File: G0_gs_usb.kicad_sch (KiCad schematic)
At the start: 59 parts, among them J1 USB_C_Receptacle_USB2.0, J12 CAN1, J13 CAN2, J4 Conn_01x03_Pin, SW1 SW_Push_Dual, U1 STM32G0B1CBTx, U2 TJA1042T-3, U3 TJA1042T-3, U4 XC6206PxxxMR

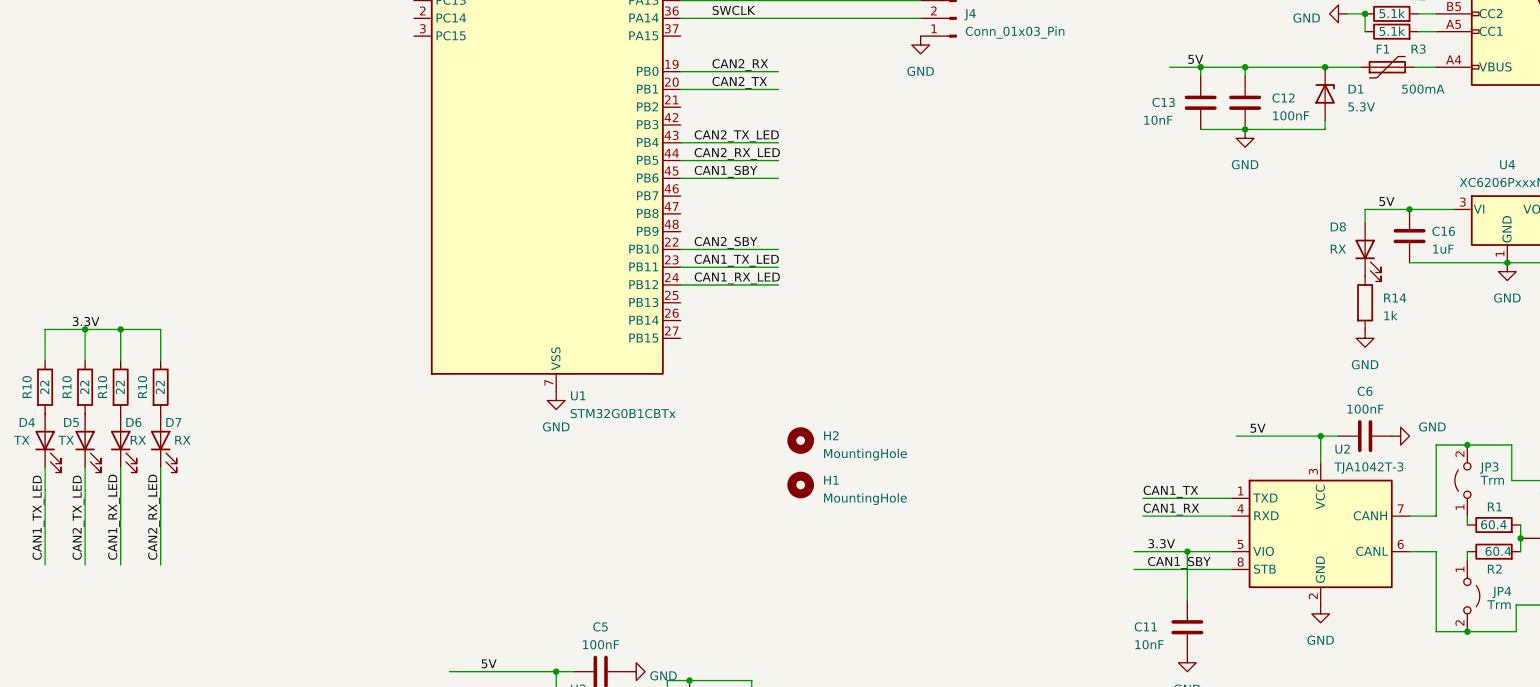
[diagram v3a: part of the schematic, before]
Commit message: Update net labels to match the purpose of the pins.
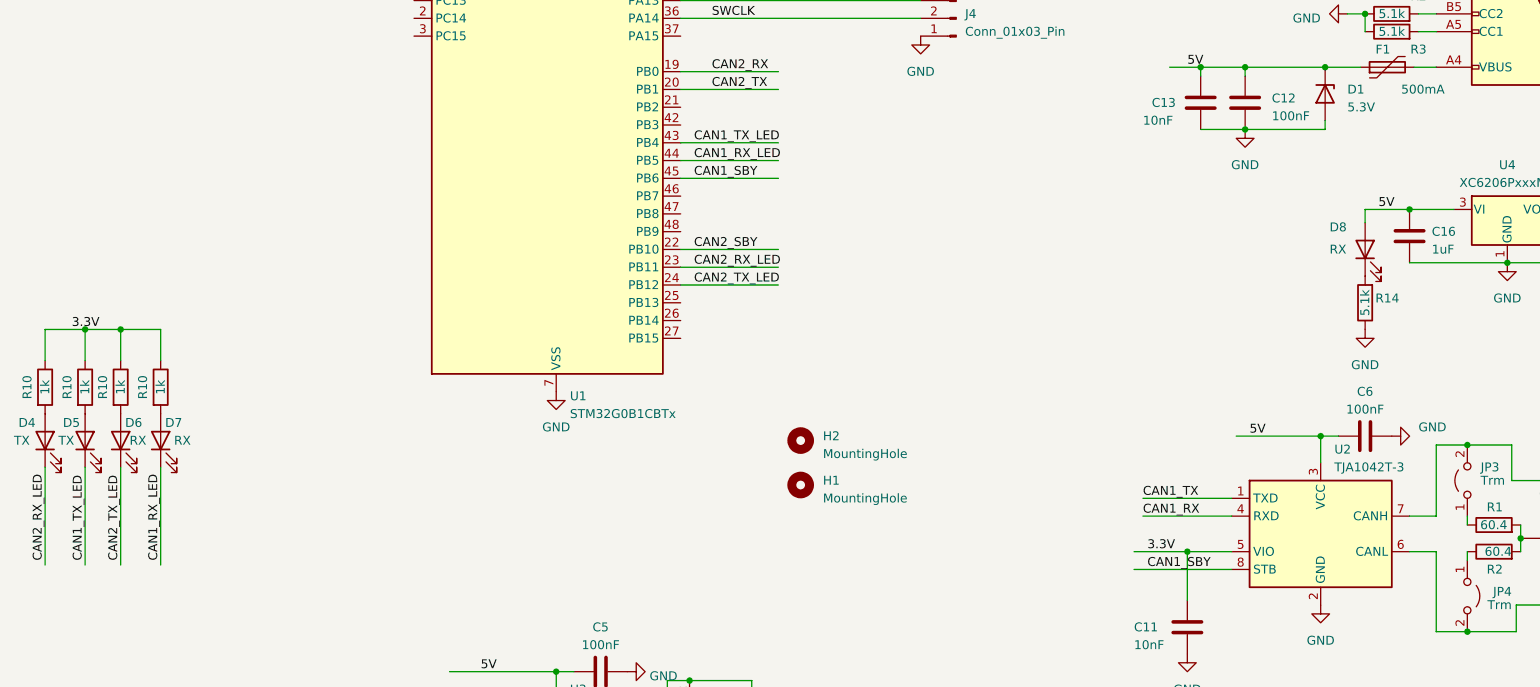
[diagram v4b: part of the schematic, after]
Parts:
- R10: value 22 -> 1k; LCSC Part # C25092 -> C11702; Part # 0402WGF220JTCE -> 0402WGF1001TCE
- R14: value 1k -> 5.1k; LCSC Part # C11702 -> C11616; Part # 0402WGF1001TCE -> 0402WGF5103TCE
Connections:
- net CAN1_RX_LED: now also D7.1 (K), U1.44 (PB5); no longer D6.1 (K), U1.24 (PB12)
- net CAN1_TX_LED: now also D5.1 (K), U1.43 (PB4); no longer D4.1 (K), U1.23 (PB11)
- net CAN2_RX_LED: now also D4.1 (K), U1.23 (PB11); no longer D7.1 (K), U1.44 (PB5)
- net CAN2_TX_LED: now also D6.1 (K), U1.24 (PB12); no longer D5.1 (K), U1.43 (PB4)
- net GND: now also R14.1; no longer R14.2
- net at D8.1 (K): now also R14.2; no longer R14.1
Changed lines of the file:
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@@
     (effects (font (size 1.27 1.27)) (justify left bottom))
   )
-  (label "CAN1_RX_LED" (at 39.37 144.145 90) (fields_autoplaced)
+  (label "CAN2_TX_LED" (at 39.37 144.145 90) (fields_autoplaced)
     (effects (font (size 1.27 1.27)) (justify left bottom))
   )
@@
     (effects (font (size 1.27 1.27)) (justify left bottom))
   )
-  (label "CAN2_RX_LED" (at 121.285 86.995 0) (fields_autoplaced)
+  (label "CAN1_RX_LED" (at 121.285 86.995 0) (fields_autoplaced)
     (effects (font (size 1.27 1.27)) (justify left bottom))
   )
@@
     (effects (font (size 1.27 1.27)) (justify left bottom))
   )
-  (label "CAN2_TX_LED" (at 121.285 84.455 0) (fields_autoplaced)
+  (label "CAN1_TX_LED" (at 121.285 84.455 0) (fields_autoplaced)
     (effects (font (size 1.27 1.27)) (justify left bottom))
   )
@@
     (effects (font (size 1.27 1.27)) (justify left bottom))
   )
-  (label "CAN1_TX_LED" (at 121.285 102.235 0) (fields_autoplaced)
+  (label "CAN2_RX_LED" (at 121.285 102.235 0) (fields_autoplaced)
     (effects (font (size 1.27 1.27)) (justify left bottom))
   )
@@
     (effects (font (size 1.27 1.27)) (justify left bottom))
   )
-  (label "CAN1_TX_LED" (at 28.575 144.145 90) (fields_autoplaced)
+  (label "CAN2_RX_LED" (at 28.575 144.145 90) (fields_autoplaced)
     (effects (font (size 1.27 1.27)) (justify left bottom))
   )
@@
     (effects (font (size 1.27 1.27)) (justify left bottom))
   )
-  (label "CAN2_TX_LED" (at 34.29 144.145 90) (fields_autoplaced)
-    (effects (font (size 1.27 1.27)) (justify left bottom))
-  )
-  (label "CAN1_RX_LED" (at 121.285 104.775 0) (fields_autoplaced)
+  (label "CAN1_TX_LED" (at 34.29 144.145 90) (fields_autoplaced)
+    (effects (font (size 1.27 1.27)) (justify left bottom))
+  )
+  (label "CAN2_TX_LED" (at 121.285 104.775 0) (fields_autoplaced)
     (effects (font (size 1.27 1.27)) (justify left bottom))
   )
@@
     (effects (font (size 1.27 1.27)) (justify left bottom))
   )
-  (label "CAN2_RX_LED" (at 45.085 144.145 90) (fields_autoplaced)
+  (label "CAN1_RX_LED" (at 45.085 144.145 90) (fields_autoplaced)
     (effects (font (size 1.27 1.27)) (justify left bottom))
   )
@@
       (effects (font (size 1.27 1.27)))
     )
-    (property "Value" "22" (at 28.575 119.38 90)
+    (property "Value" "1k" (at 28.575 119.38 90)
       (effects (font (size 1.27 1.27)))
     )
@@
       (effects (font (size 1.27 1.27)) hide)
     )
-    (property "Part #" "0402WGF220JTCE" (at 28.575 119.38 0)
-      (effects (font (size 1.27 1.27)) hide)
-    )
-    (property "LCSC Part #" "C25092" (at 28.575 119.38 0)
+    (property "Part #" "0402WGF1001TCE" (at 28.575 119.38 0)
+      (effects (font (size 1.27 1.27)) hide)
+    )
+    (property "LCSC Part #" "C11702" (at 28.575 119.38 0)
       (effects (font (size 1.27 1.27)) hide)
     )
@@
         (path "/c48c3db2-f9af-4991-ad00-70b882fee956"
           (reference "R10") (unit 1)
-        )
-      )
-    )
-  )
-  (symbol (lib_id "Device:R") (at 217.17 107.315 0) (unit 1)
-    (in_bom yes) (on_board yes) (dnp no) (fields_autoplaced)
-    (property "Reference" "R14" (at 219.71 106.68 0)
-      (effects (font (size 1.27 1.27)) (justify left))
-    )
-    (property "Value" "1k" (at 219.71 109.22 0)
-      (effects (font (size 1.27 1.27)) (justify left))
-    )
-    (property "Footprint" "Resistor_SMD:R_0402_1005Metric" (at 215.392 107.315 90)
-      (effects (font (size 1.27 1.27)) hide)
-    )
-    (property "Datasheet" "~" (at 217.17 107.315 0)
-      (effects (font (size 1.27 1.27)) hide)
-    )
-    (property "LCSC Part #" "C11702" (at 217.17 107.315 0)
-      (effects (font (size 1.27 1.27)) hide)
-    )
-    (property "Part #" "0402WGF1001TCE" (at 217.17 107.315 0)
-      (effects (font (size 1.27 1.27)) hide)
-    )
-    (pin "1")
-    (pin "2")
-    (instances
-      (project "G0_gs_usb"
-        (path "/c48c3db2-f9af-4991-ad00-70b882fee956"
-          (reference "R14") (unit 1)
         )
       )
@@
       (effects (font (size 1.27 1.27)))
     )
-    (property "Value" "22" (at 39.37 119.38 90)
+    (property "Value" "1k" (at 39.37 119.38 90)
       (effects (font (size 1.27 1.27)))
     )
@@
       (effects (font (size 1.27 1.27)) hide)
     )
-    (property "Part #" "0402WGF220JTCE" (at 39.37 119.38 0)
-      (effects (font (size 1.27 1.27)) hide)
-    )
-    (property "LCSC Part #" "C25092" (at 39.37 119.38 0)
+    (property "Part #" "0402WGF1001TCE" (at 39.37 119.38 0)
+      (effects (font (size 1.27 1.27)) hide)
+    )
+    (property "LCSC Part #" "C11702" (at 39.37 119.38 0)
       (effects (font (size 1.27 1.27)) hide)
     )
@@
       (effects (font (size 1.27 1.27)))
     )
-    (property "Value" "22" (at 34.29 119.38 90)
+    (property "Value" "1k" (at 34.29 119.38 90)
       (effects (font (size 1.27 1.27)))
     )
@@
       (effects (font (size 1.27 1.27)) hide)
     )
-    (property "Part #" "0402WGF220JTCE" (at 34.29 119.38 0)
-      (effects (font (size 1.27 1.27)) hide)
-    )
-    (property "LCSC Part #" "C25092" (at 34.29 119.38 0)
+    (property "Part #" "0402WGF1001TCE" (at 34.29 119.38 0)
+      (effects (font (size 1.27 1.27)) hide)
+    )
+    (property "LCSC Part #" "C11702" (at 34.29 119.38 0)
       (effects (font (size 1.27 1.27)) hide)
     )
@@
     )
   )
+  (symbol (lib_id "Device:R") (at 217.17 107.315 180) (unit 1)
+    (in_bom yes) (on_board yes) (dnp no)
+    (property "Reference" "R14" (at 220.345 106.68 0)
+      (effects (font (size 1.27 1.27)))
+    )
+    (property "Value" "5.1k" (at 217.17 107.315 90)
+      (effects (font (size 1.27 1.27)))
+    )
+    (property "Footprint" "Resistor_SMD:R_0402_1005Metric" (at 218.948 107.315 90)
+      (effects (font (size 1.27 1.27)) hide)
+    )
+    (property "Datasheet" "~" (at 217.17 107.315 0)
+      (effects (font (size 1.27 1.27)) hide)
+    )
+    (property "LCSC Part #" "C11616" (at 217.17 107.315 0)
+      (effects (font (size 1.27 1.27)) hide)
+    )
+    (property "Part #" "0402WGF5103TCE" (at 217.17 107.315 0)
+      (effects (font (size 1.27 1.27)) hide)
+    )
+    (pin "1")
+    (pin "2")
+    (instances
+      (project "G0_gs_usb"
+        (path "/c48c3db2-f9af-4991-ad00-70b882fee956"
+          (reference "R14") (unit 1)
+        )
+      )
+    )
+  )
   (symbol (lib_id "power:GND") (at 101.6 184.15 0) (unit 1)
     (in_bom yes) (on_board yes) (dnp no) (fields_autoplaced)
@@
       (effects (font (size 1.27 1.27)))
     )
-    (property "Value" "22" (at 45.085 119.38 90)
+    (property "Value" "1k" (at 45.085 119.38 90)
       (effects (font (size 1.27 1.27)))
     )
@@
       (effects (font (size 1.27 1.27)) hide)
     )
-    (property "Part #" "0402WGF220JTCE" (at 45.085 119.38 0)
-      (effects (font (size 1.27 1.27)) hide)
-    )
-    (property "LCSC Part #" "C25092" (at 45.085 119.38 0)
-      (effects (font (size 1.27 1.27)) hide)
-    )
+    (property "Part #" "0402WGF1001TCE" (at 45.085 119.38 0)
+      (effects (font (size 1.27 1.27)) hide)
+    )
+    (property "LCSC Part #" "C11702" (at 45.085 119.38 0)
+      (effects (font (size 1.27 1.27)) hide)
+    )
